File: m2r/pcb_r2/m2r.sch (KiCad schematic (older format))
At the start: 115 parts, among them IC1 ADP3338, IC10 STM32F303C, IC2 ADP3335, IC3 ADuM1201, IC4 ADuM1201, IC5 ADuM1201, IC6 MTX2, IC8 MAX-7Q, P1 CONN_2, P2 SMA, P3 CONN_4, P4 CONN_4, P5 CONN_4, P6 SWD, P7 SMA, P8 CONN_2, P9 CONN_2, Q1 Q_PMOS_GSD, Q2 Q_NMOS_GSD, X1 BAT BOX, X10 8M, X11 M3 MOUNT, X12 M3 MOUNT, X13 M3 MOUNT, X14 M3 MOUNT, X15 HOUSING, X2 ARM SW, X3 HOUSING, X4 HOUSING, X5 HOUSING, X6 HOUSING, X7 HOUSING, X8 RG LED, X9 HOUSING

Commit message: almost all m2r r2 routed except vcc lol
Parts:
- removed Q1: Q_PMOS_GSD, symbol Q_PMOS_GSD
- removed Q2: Q_NMOS_GSD, symbol Q_NMOS_GSD
- removed X2: ARM SW, symbol PART
- added D12, D13: CGA0402MLC-12G, m2r:R0402, symbol CGA0402MLC-12G
- added Q1: Q_PMOS_GSD_PSV, m2r:SOT-23, symbol Q_PMOS_GSD_PSV
- added Q2: Q_NMOS_GSD_PSV, m2r:SOT-23, symbol Q_NMOS_GSD_PSV
- added R16: 100, m2r:R0603, symbol R
- added TP29: TESTPAD, m2r:TESTPAD, symbol TESTPAD
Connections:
- net +5V: now also Q1.2 (S)
- net 5V_OUT: now also IC10.11 (PA1), R16.2; no longer IC10.32 (PA11)
- net GND: now also D12.2, D13.1, Q2.2 (S)
- net GPS_RESET: now also IC10.45 (PB8); no longer IC10.41 (PB5)
- net at IC8.11 (RF_IN), P2.1 (RF): now also D12.1
- net at R15.1: now also Q2.1 (G)
- net at R6.2: now also Q2.3 (D)
- net at P9.2 (PM): now also D13.2, Q1.3 (D), TP29.1 (TP)
- net SWO: no longer names the net of P6.6 (SWO/TDO)
- net SWO: no longer IC10.39 (PB3)
- new net: Q1.1 (G), R16.1
- no-connect marks 17 -> 19
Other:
- moved on the sheet: P9, R3, TP19, TP27, X15
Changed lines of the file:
@@
 LIBS:adp3335
 LIBS:cga0402mlc-12g
+LIBS:mosfet_passive
 LIBS:m2r-cache
 EELAYER 25 0
@@
 $EndComp
 $Comp
-L PART X2
-U 1 1 5378FC77
-P 1100 700
-F 0 "X2" H 1150 700 60  0000 C CNN
-F 1 "ARM SW" H 1250 800 60  0000 C CNN
-F 2 "" H 1100 700 60  0001 C CNN
-F 3 "" H 1100 700 60  0000 C CNN
-F 4 "149288" H 1100 700 60  0001 C CNN "Farnell"
-	1    1100 700
-	1    0    0    -1
-$EndComp
-$Comp
 L CONN_2 P1
 U 1 1 5378FD2B
@@
 Text GLabel 3650 2100 2    60   Output ~ 0
 SWCLK
-Text GLabel 3650 2200 2    60   Input ~ 0
-SWO
 Text GLabel 3650 2400 2    60   Output ~ 0
 nRST
@@
 Text GLabel 3350 4250 2    60   Input ~ 0
 SWCLK
-Text GLabel 3350 4800 2    60   Output ~ 0
-SWO
 Text GLabel 3350 3150 2    60   Input ~ 0
 SER_IN
@@
 Text Notes 550  6400 0    60   ~ 0
 MICROCONTROLLER
-NoConn ~ 3150 2950
+NoConn ~ 3150 3950
 NoConn ~ 3150 3650
 NoConn ~ 3150 4050
@@
 Text GLabel 9750 3300 2    60   Input ~ 0
 GPS_RESET
-Text GLabel 3350 5000 2    60   Output ~ 0
+Text GLabel 3350 5300 2    60   Output ~ 0
 GPS_RESET
 Text GLabel 8700 3150 0    60   Input ~ 0
@@
 GPS_SCL
 NoConn ~ 3150 4900
-NoConn ~ 3150 5300
+NoConn ~ 3150 5000
 Text GLabel 9550 950  0    60   Output ~ 0
 GPS_RX
@@
 L TESTPAD TP19
 U 1 1 53D0E14D
-P 3300 5000
-F 0 "TP19" H 3330 4960 30  0000 C CNN
-F 1 "TESTPAD" H 3300 5050 60  0001 C CNN
-F 2 "m2r:TESTPAD" H 3300 5000 60  0001 C CNN
-F 3 "" H 3300 5000 60  0000 C CNN
-	1    3300 5000
+P 3300 5300
+F 0 "TP19" H 3330 5260 30  0000 C CNN
+F 1 "TESTPAD" H 3300 5350 60  0001 C CNN
+F 2 "m2r:TESTPAD" H 3300 5300 60  0001 C CNN
+F 3 "" H 3300 5300 60  0000 C CNN
+	1    3300 5300
 	0    1    -1   0
 $EndComp
@@
 	3550 2400 3650 2400
 Wire Wire Line
-	3550 2200 3650 2200
-Wire Wire Line
 	3550 2100 3650 2100
 Wire Wire Line
@@
 	3150 3350 3350 3350
 Wire Wire Line
-	3150 4800 3350 4800
-Wire Wire Line
 	3150 4250 3350 4250
 Wire Wire Line
@@
 	4100 4800 4100 3600
 Wire Wire Line
-	3150 5000 3350 5000
+	3150 5300 3350 5300
 Wire Wire Line
 	3150 5100 3350 5100
@@
 Connection ~ 3300 5200
 Connection ~ 3300 5100
-Connection ~ 3300 5000
+Connection ~ 3300 5300
 Connection ~ 9600 1050
 Connection ~ 9600 950
@@
 L +5V #PWR075
 U 1 1 555DA162
-P 8050 4450
-F 0 "#PWR075" H 8050 4540 20  0001 C CNN
-F 1 "+5V" H 8050 4540 30  0000 C CNN
-F 2 "" H 8050 4450 60  0000 C CNN
-F 3 "" H 8050 4450 60  0000 C CNN
-	1    8050 4450
+P 8400 4450
+F 0 "#PWR075" H 8400 4540 20  0001 C CNN
+F 1 "+5V" H 8400 4540 30  0000 C CNN
+F 2 "" H 8400 4450 60  0000 C CNN
+F 3 "" H 8400 4450 60  0000 C CNN
+	1    8400 4450
 	1    0    0    -1
 $EndComp
@@
 L R R3
 U 1 1 555DA906
-P 7800 4500
-F 0 "R3" V 7880 4500 40  0000 C CNN
-F 1 "10k" V 7807 4501 40  0000 C CNN
-F 2 "m2r:R0603" V 7730 4500 30  0001 C CNN
-F 3 "" H 7800 4500 30  0000 C CNN
-F 4 "2332016" H 7800 4500 60  0001 C CNN "Farnell"
-	1    7800 4500
+P 8150 4500
+F 0 "R3" V 8230 4500 40  0000 C CNN
+F 1 "10k" V 8157 4501 40  0000 C CNN
+F 2 "m2r:R0603" V 8080 4500 30  0001 C CNN
+F 3 "" H 8150 4500 30  0000 C CNN
+F 4 "2332016" H 8150 4500 60  0001 C CNN "Farnell"
+	1    8150 4500
 	0    1    1    0
 $EndComp
 Wire Wire Line
-	8050 4450 8050 4550
+	8400 4450 8400 4550
 Wire Wire Line
-	7950 4500 8050 4500
-Connection ~ 8050 4500
+	8300 4500 8400 4500
+Connection ~ 8400 4500
 Wire Wire Line
 	7600 4750 7750 4750
@@
 L CONN_2 P9
 U 1 1 555DBB15
-P 8500 5100
-F 0 "P9" V 8450 5100 40  0000 C CNN
-F 1 "CONN_2" V 8550 5100 40  0000 C CNN
-F 2 "m2r:S02B-PASK-2" H 8500 5100 60  0001 C CNN
-F 3 "" H 8500 5100 60  0000 C CNN
-F 4 "1830747" H 8500 5100 60  0001 C CNN "Farnell"
-	1    8500 5100
+P 8850 5100
+F 0 "P9" V 8800 5100 40  0000 C CNN
+F 1 "CONN_2" V 8900 5100 40  0000 C CNN
+F 2 "m2r:S02B-PASK-2" H 8850 5100 60  0001 C CNN
+F 3 "" H 8850 5100 60  0000 C CNN
+F 4 "1830747" H 8850 5100 60  0001 C CNN "Farnell"
+	1    8850 5100
 	1    0    0    1
 $EndComp
@@
 L PART X15
 U 1 1 555DBC69
-P 8700 5100
-F 0 "X15" H 8750 5100 60  0000 C CNN
-F 1 "HOUSING" H 8900 5200 60  0000 C CNN
-F 2 "" H 8700 5100 60  0001 C CNN
-F 3 "" H 8700 5100 60  0000 C CNN
-F 4 "1830726" H 8700 5100 60  0001 C CNN "Farnell"
-	1    8700 5100
+P 9050 5100
+F 0 "X15" H 9100 5100 60  0000 C CNN
+F 1 "HOUSING" H 9250 5200 60  0000 C CNN
+F 2 "" H 9050 5100 60  0001 C CNN
+F 3 "" H 9050 5100 60  0000 C CNN
+F 4 "1830726" H 9050 5100 60  0001 C CNN "Farnell"
+	1    9050 5100
 	1    0    0    -1
 $EndComp
 Wire Wire Line
-	8050 4950 8050 5000
+	8400 4950 8400 5000
 Wire Wire Line
-	8050 5000 8150 5000
+	8300 5000 8500 5000
 $Comp
 L GND #PWR076
 U 1 1 555DC0CC
-P 8050 5250
-F 0 "#PWR076" H 8050 5250 30  0001 C CNN
-F 1 "GND" H 8050 5180 30  0001 C CNN
-F 2 "" H 8050 5250 60  0000 C CNN
-F 3 "" H 8050 5250 60  0000 C CNN
-	1    8050 5250
+P 8400 5250
+F 0 "#PWR076" H 8400 5250 30  0001 C CNN
+F 1 "GND" H 8400 5180 30  0001 C CNN
+F 2 "" H 8400 5250 60  0000 C CNN
+F 3 "" H 8400 5250 60  0000 C CNN
+	1    8400 5250
 	1    0    0    -1
 $EndComp
 Wire Wire Line
-	8150 5200 8050 5200
+	8500 5200 8400 5200
 Wire Wire Line
-	8050 5200 8050 5250
+	8400 5200 8400 5250
 Wire Notes Line
 	4100 4850 4100 6450
@@
 Text GLabel 3350 5400 2    60   Input ~ 0
 BUZZER
-Text GLabel 3350 3950 2    60   Input ~ 0
+Text GLabel 3350 2950 2    60   Input ~ 0
 5V_OUT
 Connection ~ 3300 3250
@@
 Connection ~ 3300 5400
 Wire Wire Line
-	3150 3950 3350 3950
+	3150 2950 3350 2950
 $Comp
 L TESTPAD TP27
 U 1 1 555E38F4
-P 3300 3950
-F 0 "TP27" H 3330 3910 30  0000 C CNN
-F 1 "TESTPAD" H 3300 4000 60  0001 C CNN
-F 2 "m2r:TESTPAD" H 3300 3950 60  0001 C CNN
-F 3 "" H 3300 3950 60  0000 C CNN
-	1    3300 3950
+P 3300 2950
+F 0 "TP27" H 3330 2910 30  0000 C CNN
+F 1 "TESTPAD" H 3300 3000 60  0001 C CNN
+F 2 "m2r:TESTPAD" H 3300 2950 60  0001 C CNN
+F 3 "" H 3300 2950 60  0000 C CNN
+	1    3300 2950
 	0    1    -1   0
 $EndComp
-Connection ~ 3300 3950
+Connection ~ 3300 2950
 Wire Wire Line
 	3150 3450 3350 3450
@@
 NoConn ~ 3150 5600
 $Comp
-L Q_NMOS_GSD Q2
-U 1 1 555D2141
+L Q_NMOS_GSD_PSV Q2
+U 1 1 555D254C
 P 5550 5900
 F 0 "Q2" H 5850 5950 50  0000 R CNN
-F 1 "Q_NMOS_GSD" H 6200 5850 50  0000 R CNN
-F 2 "" H 5750 6000 29  0000 C CNN
+F 1 "Q_NMOS_GSD_PSV" H 6400 5850 50  0000 R CNN
+F 2 "m2r:SOT-23" H 5750 6000 29  0001 C CNN
 F 3 "" H 5550 5900 60  0000 C CNN
+F 4 "1510761" H 5550 5900 60  0001 C CNN "Farnell"
 	1    5550 5900
 	1    0    0    -1
 $EndComp
 $Comp
-L Q_PMOS_GSD Q1
-U 1 1 555D29BA
-P 7950 4750
-F 0 "Q1" H 8250 4800 50  0000 R CNN
-F 1 "Q_PMOS_GSD" H 8600 4700 50  0000 R CNN
-F 2 "" H 8150 4850 29  0000 C CNN
-F 3 "" H 7950 4750 60  0000 C CNN
-	1    7950 4750
+L Q_PMOS_GSD_PSV Q1
+U 1 1 555D2A89
+P 8300 4750
+F 0 "Q1" H 8600 4800 50  0000 R CNN
+F 1 "Q_PMOS_GSD_PSV" H 9150 4700 50  0000 R CNN
+F 2 "m2r:SOT-23" H 8500 4850 29  0001 C CNN
+F 3 "" H 8300 4750 60  0000 C CNN
+F 4 "1894738" H 8300 4750 60  0001 C CNN "Farnell"
+	1    8300 4750
 	1    0    0    1
 $EndComp
+$Comp
+L CGA0402MLC-12G D12
+U 1 1 555D4F9B
+P 10050 2300
+F 0 "D12" H 10150 2200 60  0000 C CNN
+F 1 "CGA0402MLC-12G" H 10150 2410 60  0001 C CNN
+F 2 "m2r:R0402" H 10050 2300 10  0001 C CNN
+F 3 "" H 10050 2300 60  0000 C CNN
+F 4 "2368169" H 10050 2300 60  0001 C CNN "Farnell"
+	1    10050 2300
+	0    1    1    0
+$EndComp
+Wire Wire Line
+	10050 2250 10050 2300
+Connection ~ 10050 2250
+$Comp
+L GND #PWR077
+U 1 1 555D537B
+P 10050 2550
+F 0 "#PWR077" H 10050 2550 30  0001 C CNN
+F 1 "GND" H 10050 2480 30  0001 C CNN
+F 2 "" H 10050 2550 60  0000 C CNN
+F 3 "" H 10050 2550 60  0000 C CNN
+	1    10050 2550
+	1    0    0    -1
+$EndComp
+Wire Wire Line
+	10050 2500 10050 2550
+$Comp
+L R R16
+U 1 1 555D638E
+P 7900 4750
+F 0 "R16" V 7980 4750 40  0000 C CNN
+F 1 "100" V 7907 4751 40  0000 C CNN
+F 2 "m2r:R0603" V 7830 4750 30  0001 C CNN
+F 3 "" H 7900 4750 30  0000 C CNN
+F 4 "2331989" H 7900 4750 60  0001 C CNN "Farnell"
+	1    7900 4750
+	0    1    1    0
+$EndComp
+Wire Wire Line
+	8050 4750 8100 4750
+Wire Wire Line
+	7650 4500 8000 4500
+$Comp
+L TESTPAD TP29
+U 1 1 555D8FAC
+P 8300 5000
+F 0 "TP29" H 8330 4960 30  0000 C CNN
+F 1 "TESTPAD" H 8300 5050 60  0001 C CNN
+F 2 "m2r:TESTPAD" H 8300 5000 60  0001 C CNN
+F 3 "" H 8300 5000 60  0000 C CNN
+	1    8300 5000
+	0    -1   1    0
+$EndComp
+NoConn ~ 3550 2200
+NoConn ~ 3150 4800
+$Comp
+L CGA0402MLC-12G D13
+U 1 1 555D91C7
+P 8450 5200
+F 0 "D13" H 8550 5100 60  0000 C CNN
+F 1 "CGA0402MLC-12G" H 8550 5310 60  0001 C CNN
+F 2 "m2r:R0402" H 8450 5200 10  0001 C CNN
+F 3 "" H 8450 5200 60  0000 C CNN
+F 4 "2368169" H 8450 5200 60  0001 C CNN "Farnell"
+	1    8450 5200
+	0    -1   -1   0
+$EndComp
+Connection ~ 8450 5200
+Connection ~ 8450 5000
+Connection ~ 8400 5000
 $EndSCHEMATC

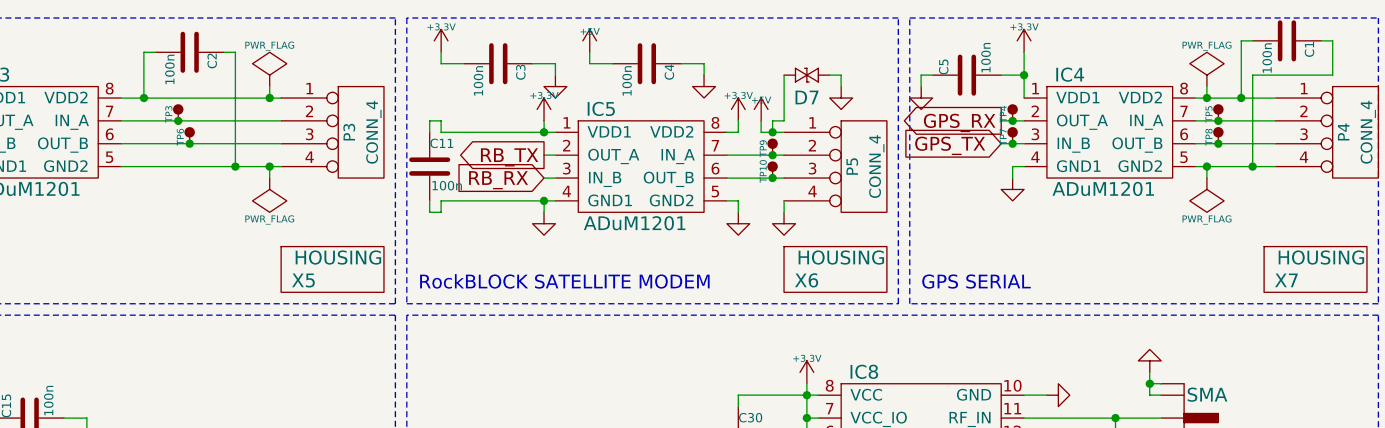
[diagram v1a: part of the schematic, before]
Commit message: finished up routing, done silk
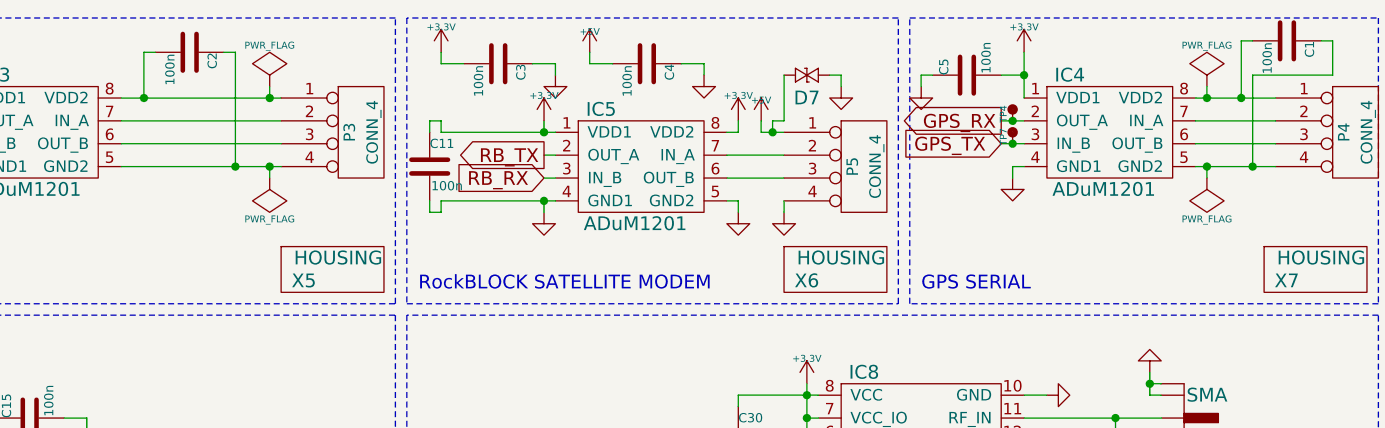
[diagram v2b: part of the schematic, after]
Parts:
- removed TP10, TP3, TP5, TP6, TP8, TP9: TESTPAD, m2r:TESTPAD, symbol TESTPAD
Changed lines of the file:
@@
 	1    0    0    1
-$EndComp
-$Comp
-L TESTPAD TP3
-U 1 1 537F5E03
-P 5950 950
-F 0 "TP3" H 5980 910 30  0000 C CNN
-F 1 "TESTPAD" H 5950 1000 60  0001 C CNN
-F 2 "m2r:TESTPAD" H 5950 950 60  0001 C CNN
-F 3 "" H 5950 950 60  0000 C CNN
-	1    5950 950
-	0    1    -1   0
-$EndComp
-$Comp
-L TESTPAD TP6
-U 1 1 537F61C5
-P 6000 1050
-F 0 "TP6" H 6030 1010 30  0000 C CNN
-F 1 "TESTPAD" H 6000 1100 60  0001 C CNN
-F 2 "m2r:TESTPAD" H 6000 1050 60  0001 C CNN
-F 3 "" H 6000 1050 60  0000 C CNN
-	1    6000 1050
-	0    1    -1   0
-$EndComp
-$Comp
-L TESTPAD TP9
-U 1 1 537F62C4
-P 8550 1100
-F 0 "TP9" H 8580 1060 30  0000 C CNN
-F 1 "TESTPAD" H 8550 1150 60  0001 C CNN
-F 2 "m2r:TESTPAD" H 8550 1100 60  0001 C CNN
-F 3 "" H 8550 1100 60  0000 C CNN
-	1    8550 1100
-	0    1    -1   0
-$EndComp
-$Comp
-L TESTPAD TP10
-U 1 1 537F66DE
-P 8550 1200
-F 0 "TP10" H 8580 1160 30  0000 C CNN
-F 1 "TESTPAD" H 8550 1250 60  0001 C CNN
-F 2 "m2r:TESTPAD" H 8550 1200 60  0001 C CNN
-F 3 "" H 8550 1200 60  0000 C CNN
-	1    8550 1200
-	0    1    -1   0
 $EndComp
 Text GLabel 4750 2700 0    60   Input ~ 0
@@
 $EndComp
 $Comp
-L TESTPAD TP5
-U 1 1 53D0016C
-P 10500 950
-F 0 "TP5" H 10530 910 30  0000 C CNN
-F 1 "TESTPAD" H 10500 1000 60  0001 C CNN
-F 2 "m2r:TESTPAD" H 10500 950 60  0001 C CNN
-F 3 "" H 10500 950 60  0000 C CNN
-	1    10500 950
-	0    1    -1   0
-$EndComp
-$Comp
 L PART X7
 U 1 1 53D00179
@@
 	1    9200 800
 	1    0    0    -1
-$EndComp
-$Comp
-L TESTPAD TP8
-U 1 1 53D05E00
-P 10500 1050
-F 0 "TP8" H 10530 1010 30  0000 C CNN
-F 1 "TESTPAD" H 10500 1100 60  0001 C CNN
-F 2 "m2r:TESTPAD" H 10500 1050 60  0001 C CNN
-F 3 "" H 10500 1050 60  0000 C CNN
-	1    10500 1050
-	0    1    -1   0
 $EndComp
 $Comp
@@
 	3850 850  3850 900
 Connection ~ 3850 900
-Connection ~ 5950 950
-Connection ~ 6000 1050
-Connection ~ 8550 1200
-Connection ~ 8550 1100
 Connection ~ 3300 3350
 Connection ~ 3300 3750
@@
 Wire Notes Line
 	9150 1750 9150 500
-Connection ~ 10500 950
-Connection ~ 10500 1050
 Wire Wire Line
 	3350 5700 3150 5700

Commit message: routing updates
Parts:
- D1, D2: value RED -> GRN; Farnell 2290329 -> 2290328
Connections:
- net nRST: now also IC10.29 (PA8)
- no-connect marks 19 -> 18
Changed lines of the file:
@@
 MICROCONTROLLER
 NoConn ~ 3150 3950
-NoConn ~ 3150 3650
 NoConn ~ 3150 4050
 NoConn ~ 3150 4350
@@
 P 5100 3850
 F 0 "D1" H 5100 3950 50  0000 C CNN
-F 1 "RED" H 5100 3750 50  0000 C CNN
+F 1 "GRN" H 5100 3750 50  0000 C CNN
 F 2 "m2r:LED0603" H 5100 3850 60  0001 C CNN
 F 3 "" H 5100 3850 60  0000 C CNN
-F 4 "2290329" H 5100 3850 60  0001 C CNN "Farnell"
+F 4 "2290328" H 5100 3850 60  0001 C CNN "Farnell"
 	1    5100 3850
 	1    0    0    -1
@@
 P 6450 3850
 F 0 "D2" H 6450 3950 50  0000 C CNN
-F 1 "RED" H 6450 3750 50  0000 C CNN
+F 1 "GRN" H 6450 3750 50  0000 C CNN
 F 2 "m2r:LED0603" H 6450 3850 60  0001 C CNN
 F 3 "" H 6450 3850 60  0000 C CNN
-F 4 "2290329" H 6450 3850 60  0001 C CNN "Farnell"
+F 4 "2290328" H 6450 3850 60  0001 C CNN "Farnell"
 	1    6450 3850
 	1    0    0    -1
@@
 Connection ~ 8450 5000
 Connection ~ 8400 5000
+Text GLabel 3350 3650 2    60   Input ~ 0
+nRST
+Wire Wire Line
+	3150 3650 3350 3650
 $EndSCHEMATC

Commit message: add boms/zips for manufacture
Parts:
- P3, P4, P5: Farnell (none) -> 1830749
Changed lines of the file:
@@
 F 2 "m2r:S04B-PASK-2" H 6750 1000 60  0001 C CNN
 F 3 "" H 6750 1000 60  0000 C CNN
-F 4 "512-8484" V 6750 1000 60  0001 C CNN "RS"
+F 4 "1830749" H 6750 1000 60  0001 C CNN "Farnell"
+F 5 "512-8484" V 6750 1000 60  0001 C CNN "RS"
 	1    6750 1000
 	1    0    0    -1
@@
 F 2 "m2r:S04B-PASK-2" H 8950 1150 60  0001 C CNN
 F 3 "" H 8950 1150 60  0000 C CNN
-F 4 "512-8484" V 8950 1150 60  0001 C CNN "RS"
+F 4 "1830749" H 8950 1150 60  0001 C CNN "Farnell"
+F 5 "512-8484" V 8950 1150 60  0001 C CNN "RS"
 	1    8950 1150
 	1    0    0    -1
@@
 F 2 "m2r:S04B-PASK-2" H 11100 1000 60  0001 C CNN
 F 3 "" H 11100 1000 60  0000 C CNN
-F 4 "512-8484" V 11100 1000 60  0001 C CNN "RS"
+F 4 "1830749" H 11100 1000 60  0001 C CNN "Farnell"
+F 5 "512-8484" V 11100 1000 60  0001 C CNN "RS"
 	1    11100 1000
 	1    0    0    -1
